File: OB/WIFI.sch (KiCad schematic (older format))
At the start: 26 parts

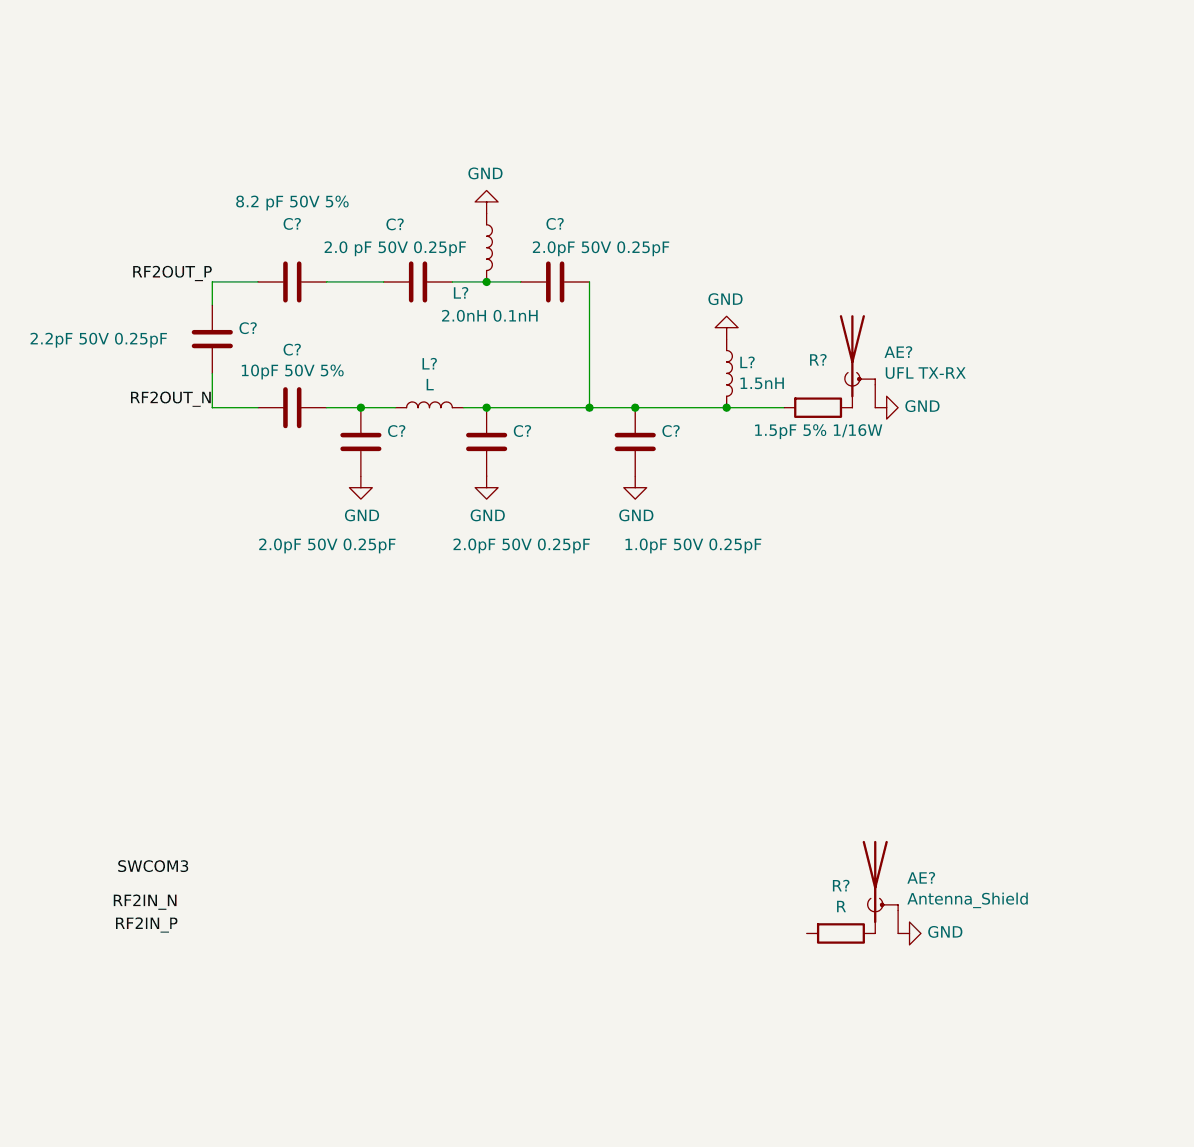
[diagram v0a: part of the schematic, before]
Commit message: wifi progress on antenna
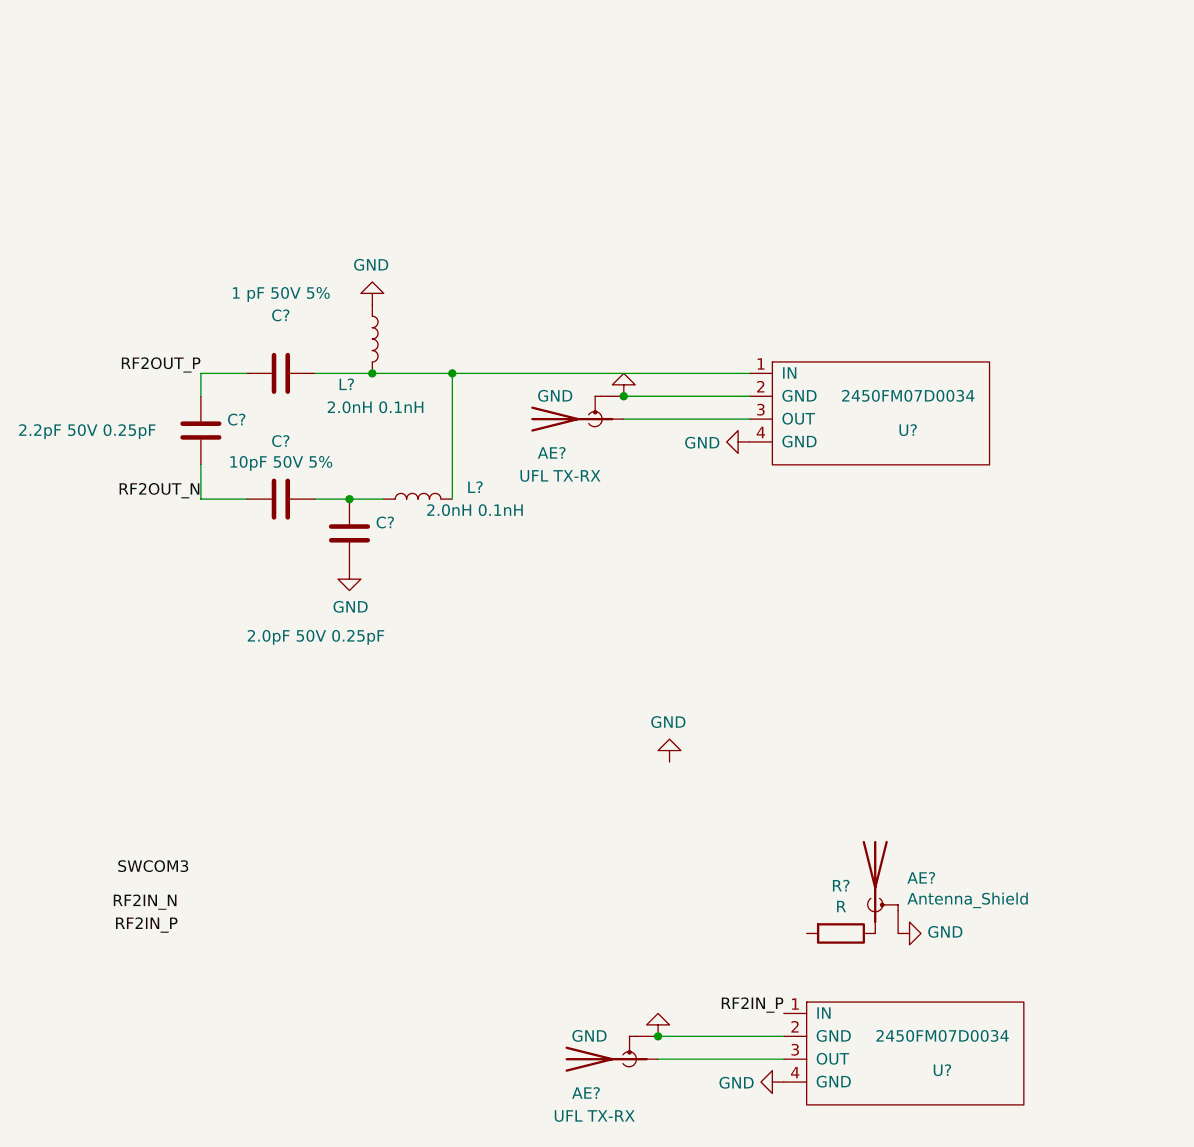
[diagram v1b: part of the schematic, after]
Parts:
- removed AE?: UFL TX-RX, symbol Device:Antenna_Shield
- removed C?: 2.0 pF 50V 0.25pF, symbol Device:C
- removed C? (x2): 2.0pF 50V 0.25pF, symbol Device:C
- removed C?: 1.0pF 50V 0.25pF, symbol Device:C
- removed L?: 1.5nH, symbol Device:L
- removed R?: 1.5pF 5% 1/16W, symbol Device:R
- added AE? (x2): UFL TX-RX, symbol Device:Antenna_Shield
- added U? (x2): 2450FM07D0034, symbol Balun:2450FM07D0034
- C?: value 8.2 pF 50V 5% -> 1 pF 50V 5%
- L?: value L -> 2.0nH 0.1nH
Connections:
- net GND: now also AE?.2 (Shield), AE?.2 (Shield), U?.2 (GND), U?.2 (GND), U?.4 (GND), U?.4 (GND)
- net RF2IN_P: now also U?.1 (IN)
- net at C?.1: now also L?.2, L?.2, U?.1 (IN)
- new net: AE?.1 (A), U?.3 (OUT) (x2)
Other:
- moved on the sheet: C?, L?

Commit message: wifi antenna done
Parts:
- removed AE?: Antenna_Shield, symbol Device:Antenna_Shield
- removed R?: R, symbol Device:R
- added C? (x2): 4.7pF, symbol Device:C
- added C?: 1.5pF 50V 0.25pF, symbol Device:C
- added C?: 1.5pF, symbol Device:C
- added C?: 10pF, symbol Device:C
- added C? (x4): 100pF, symbol Device:C
- added C? (x4): 0.1uF, symbol Device:C
- added D?: SMP1321, symbol Device:D
- added L? (x2): 2.2nH 0.1nH, symbol Device:L
- added R?: 1K, symbol Device:R
- AE?: value UFL TX-RX -> RX
- U? (x2): symbol Balun:2450FM07D0034 -> OB-rescue:2450FM07D0034-Balun
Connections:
- net GND is gone; now on net +3V3: AE?.2 (Shield), AE?.2 (Shield), C?.2, C?.2, C?.2, C?.2, L?.1, R?.1, R?.2, R?.2, U?.2 (GND), U?.2 (GND), U?.4 (GND), U?.4 (GND), U?.69 (EP)
- net +1V2: now also C?.1, C?.1, C?.1, C?.1
- net +3V3: now also C?.1, C?.1, C?.1, C?.1, C?.1, C?.1, C?.2, C?.2, C?.2, C?.2, C?.2, C?.2, C?.2, C?.2, D?.1 (K), L?.2
- net RF2IN_N: now also C?.2
- net RF2IN_P: now also C?.2; no longer U?.1 (IN)
- net SWCOM3: now also C?.2, R?.1
- new net: C?.1, C?.2, L?.1 (x2)
- new net: C?.1, D?.2 (A), L?.2, R?.2, U?.1 (IN)
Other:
- moved on the sheet: AE?, C?, L?, U?

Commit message: SmartBridgeMicro Schematic done
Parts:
- added R? (x3): 10K, symbol Device:R
- added U?: IS24C, symbol Memory:IS24C
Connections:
- net +3V3: now also R?.1, R?.1, R?.1, U?.8 (VCC); no longer AE?.2 (Shield), AE?.2 (Shield), C?.1, C?.1, C?.2, C?.2, C?.2, C?.2, C?.2, C?.2, C?.2, C?.2, C?.2, C?.2, C?.2, C?.2, D?.1 (K), L?.1, L?.2, R?.1, R?.2, R?.2, U?.2 (GND), U?.2 (GND), U?.4 (GND), U?.4 (GND), U?.69 (EP)
- net WP: now reaches U?.23 (GPIO3_EPRM_WP)
- net WP: now also R?.2, U?.7 (WP)
- net SDA: now reaches U?.24 (EPRM_SDA)
- net SDA: now also R?.2, U?.5 (SDA)
- net SCL: now reaches U?.25 (EPRM_SCK)
- net SCL: now also R?.2, U?.6 (SCL)
- new net GND: AE?.2 (Shield), AE?.2 (Shield), C?.1, C?.1, C?.2, C?.2, C?.2, C?.2, C?.2, C?.2, C?.2, C?.2, C?.2, C?.2, C?.2, C?.2, D?.1 (K), L?.1, L?.2, R?.1, R?.2, R?.2, U?.1 (A0), U?.2 (A1), U?.2 (GND), U?.2 (GND), U?.3 (A2), U?.4 (GND), U?.4 (GND), U?.4 (GND), U?.69 (EP)
- no-connect marks 19 -> 21
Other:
- note added: "NC"
- moved on the sheet: AE?, C?, L?, U?, Y?

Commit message: +esp32picod4 +fix mounting hole position -ceramic antenna +ufl -spi flash
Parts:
- removed C?: 0.1uF, symbol Device:C
- removed C?: 100pF, symbol Device:C
- removed R? (x2): 0, symbol Device:R
- C12, C13, C14, C15, C16, C17, C18, C19, C20, C21, C22, C23, C24, C25, C26, C27, C28, C29: renamed from C?; footprint (none) -> Capacitor_SMD:C_0402_1005Metric
- L5, L6, L7, L8: renamed from L?; footprint (none) -> Inductor_SMD:L_0201_0603Metric
- R15: renamed from R?; value 1K -> 2K; footprint (none) -> Resistor_SMD:R_0402_1005Metric
- R18, R19, R21, R22, R24: renamed from R?; value 10K -> 2K; footprint (none) -> Resistor_SMD:R_0402_1005Metric
- R23, R25: renamed from R?; footprint (none) -> Resistor_SMD:R_0402_1005Metric
- gave numbers to parts that had none: 8
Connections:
- net USB_D_N: now also U7.40 (DM)
- net USB_D_P: now also U7.38 (DP)
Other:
- moved on the sheet: C23, R22, R23, R24, R25, U7
